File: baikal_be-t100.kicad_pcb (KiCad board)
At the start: 4 copper layers, 95.9 x 90.2 mm, 2 parts, among them J1 2-2013289-1

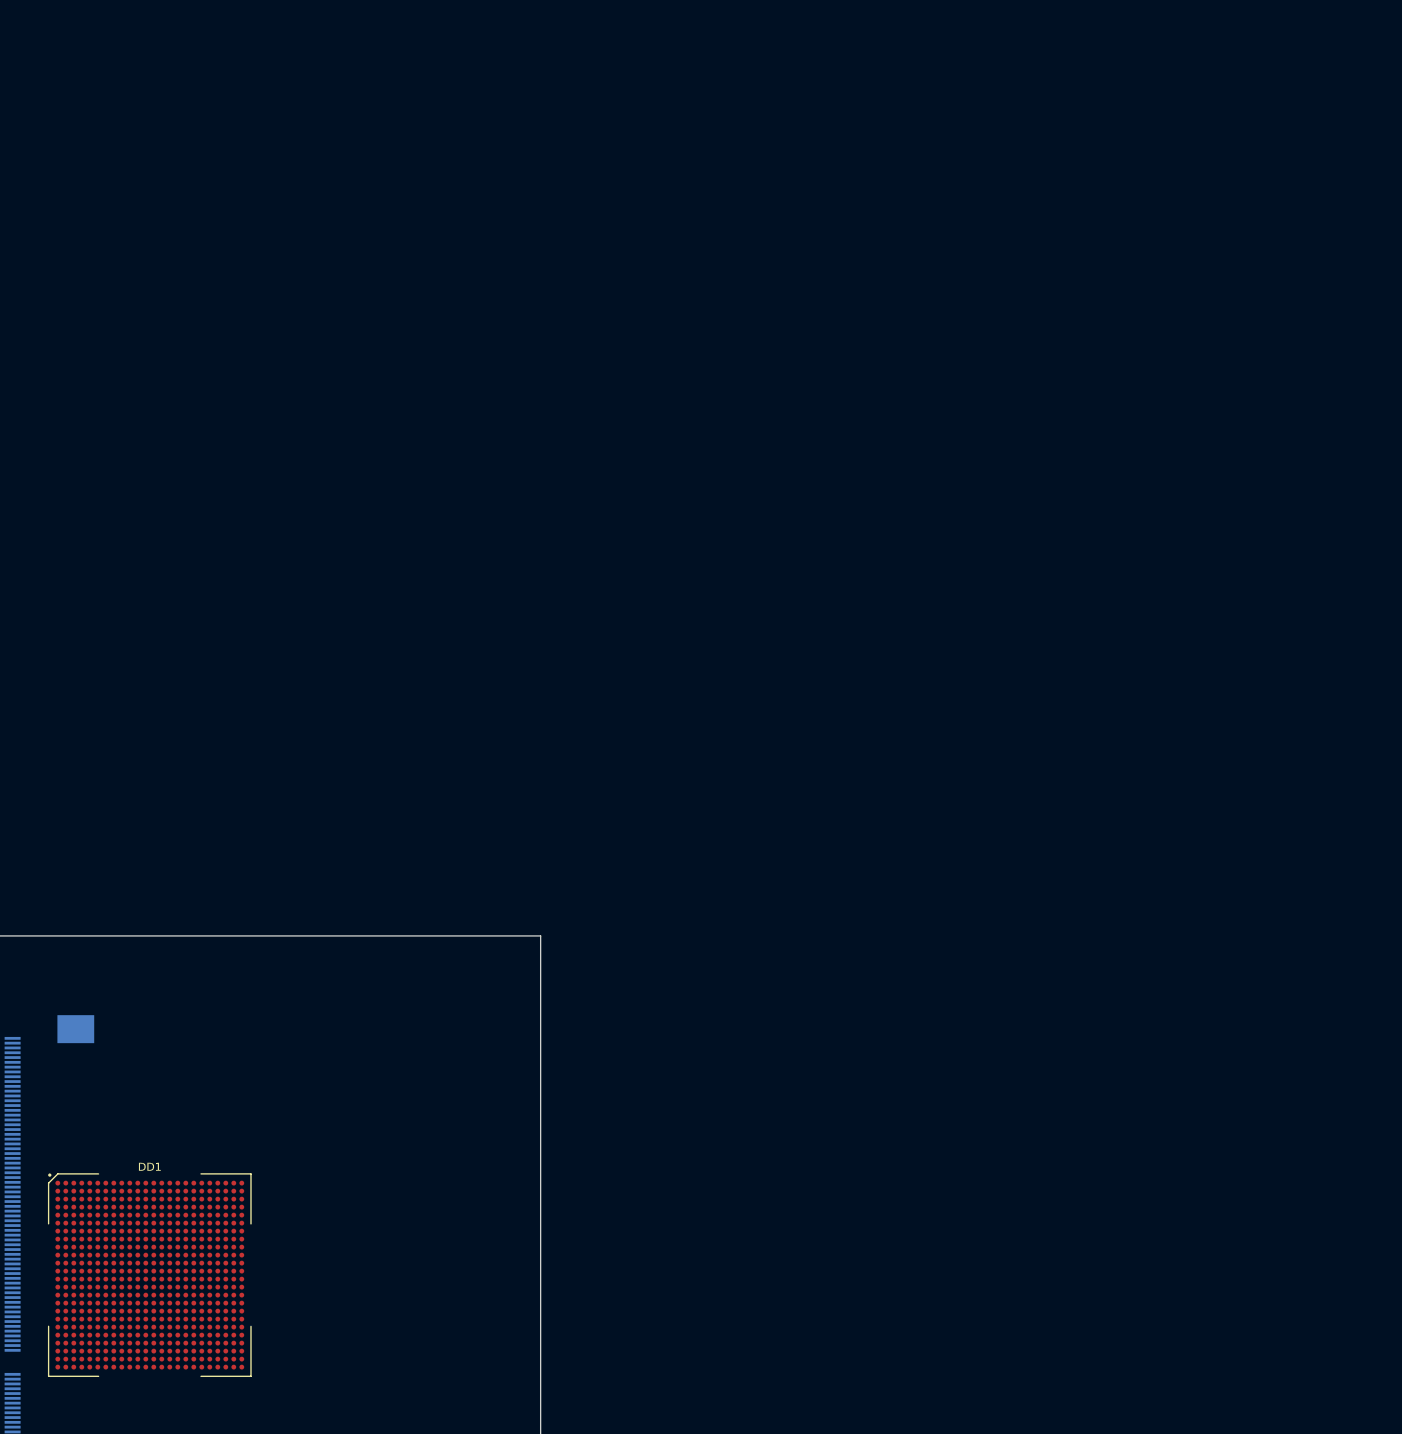
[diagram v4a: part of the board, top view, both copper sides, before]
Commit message: Changes in TRACE, EJTAG, JTAG... Updated CPU symbol.
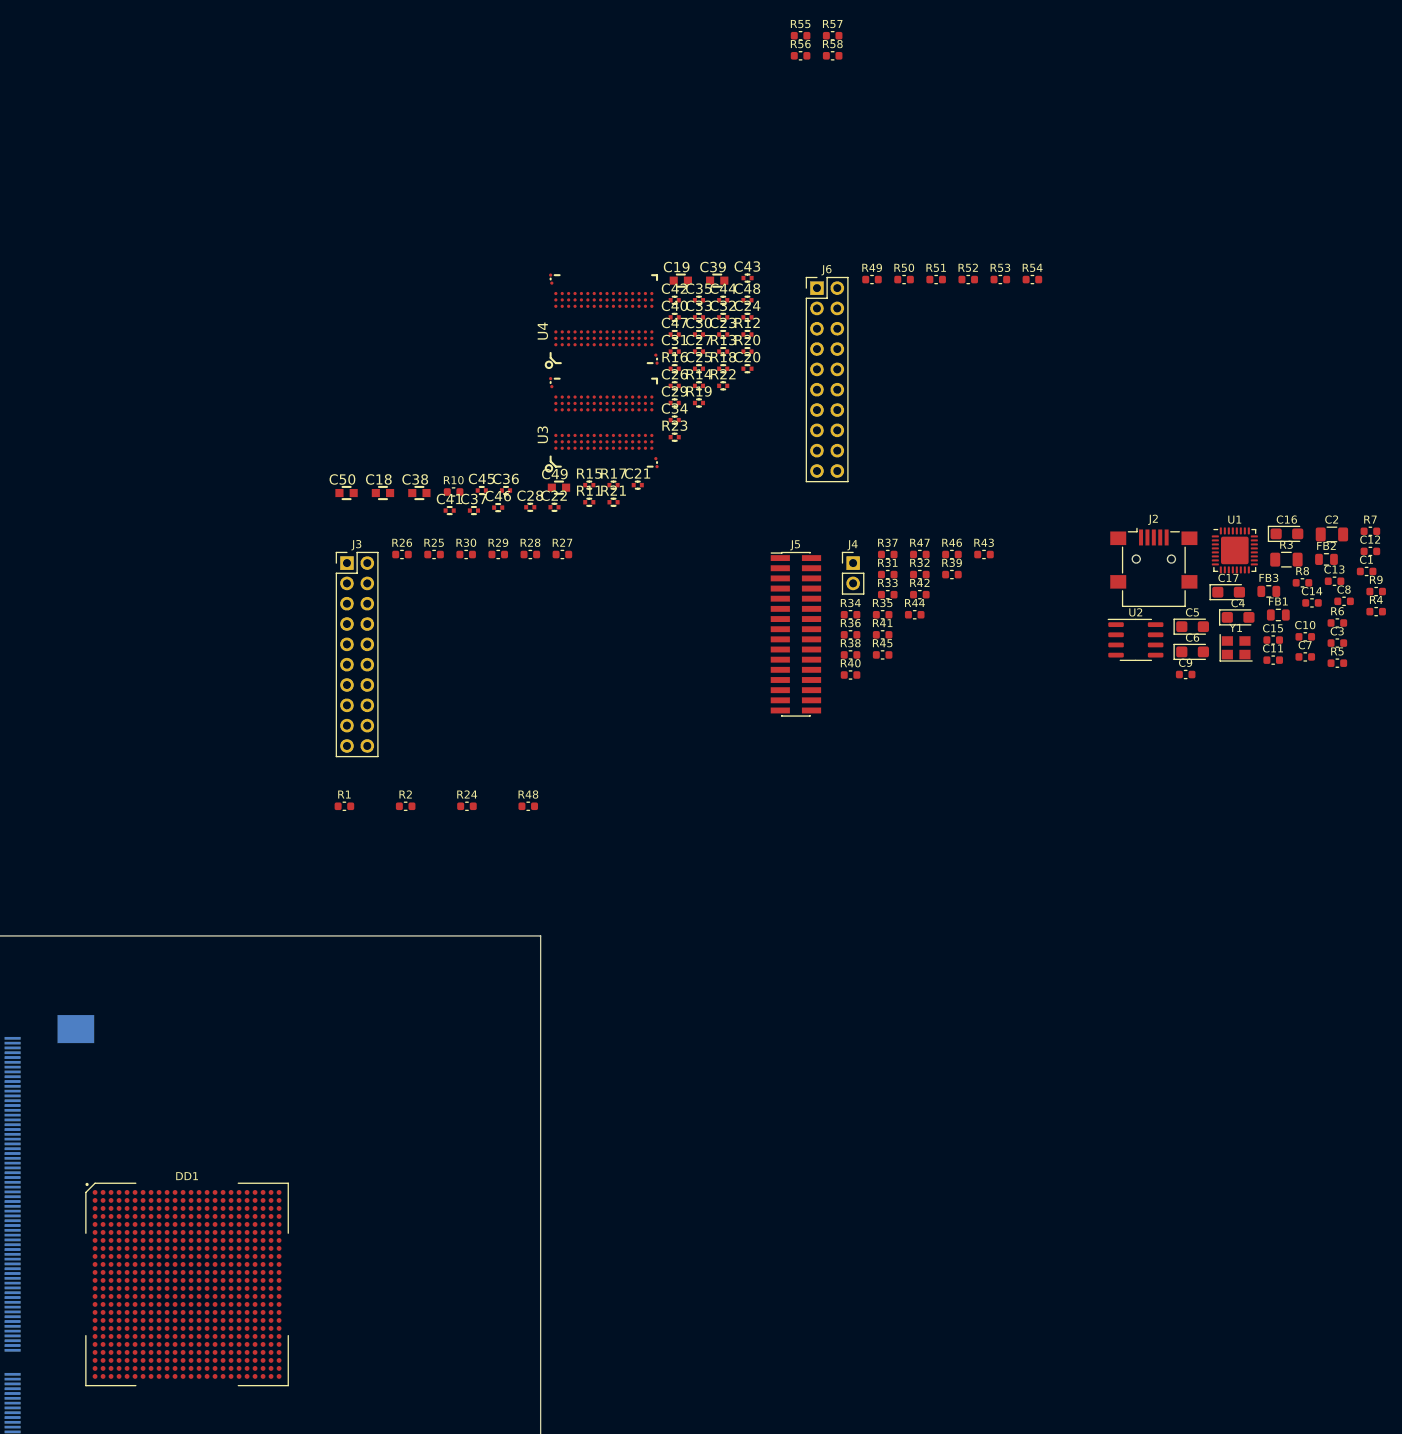
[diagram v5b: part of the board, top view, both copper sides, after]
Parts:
- added C1: 33pF, Capacitor_SMD:C_0603_1608Metric, F.Cu at (103.3, -135.7)
- added C10: 0.01uF, Capacitor_SMD:C_0603_1608Metric, F.Cu at (95.6, -127.6)
- added C11: 0.01uF, Capacitor_SMD:C_0603_1608Metric, F.Cu at (91.6, -124.6)
- added C12: 0.1uF, Capacitor_SMD:C_0603_1608Metric, F.Cu at (103.7, -138.2)
- added C13: 0.1uF, Capacitor_SMD:C_0603_1608Metric, F.Cu at (99.2, -134.5)
- added C14: 0.1uF, Capacitor_SMD:C_0603_1608Metric, F.Cu at (96.4, -131.8)
- added C15: 0.1uF, Capacitor_SMD:C_0603_1608Metric, F.Cu at (91.6, -127.2)
- added C16: 4.7uF/6.3V, Capacitor_Tantalum_SMD:CP_EIA-3216-18_Kemet-A, F.Cu at (93.3, -140.4)
- added C17: 4.7uF/6.3V, Capacitor_Tantalum_SMD:CP_EIA-3216-18_Kemet-A, F.Cu at (86.0, -133.1)
- added C18: 10uF/6.3V/20%, OLIMEX_RLC-FP:C_0603_5MIL_DWS, F.Cu at (-19.7, -145.5)
- added C19: 1uF/10V/10%, OLIMEX_RLC-FP:C_0603_5MIL_DWS, F.Cu at (17.5, -172.1)
- added C2: 0.1uF, Capacitor_SMD:C_1206_3216Metric, F.Cu at (98.9, -140.4)
- added C20: 100nF/10V/10%, OLIMEX_RLC-FP:C_0402_5MIL_DWS, F.Cu at (25.9, -161.1)
- added C21: 100nF/10V/10%, OLIMEX_RLC-FP:C_0402_5MIL_DWS, F.Cu at (12.1, -146.5)
- added C22: 100nF/10V/10%, OLIMEX_RLC-FP:C_0402_5MIL_DWS, F.Cu at (1.73, -143.8)
- added C23: 100nF/10V/10%, OLIMEX_RLC-FP:C_0402_5MIL_DWS, F.Cu at (22.8, -165.4)
- added C24: 100nF/10V/10%, OLIMEX_RLC-FP:C_0402_5MIL_DWS, F.Cu at (25.9, -167.5)
- added C25: 100nF/10V/10%, OLIMEX_RLC-FP:C_0402_5MIL_DWS, F.Cu at (19.8, -161.1)
- added C26: 100nF/10V/10%, OLIMEX_RLC-FP:C_0402_5MIL_DWS, F.Cu at (16.8, -158.9)
- added C27: 100nF/10V/10%, OLIMEX_RLC-FP:C_0402_5MIL_DWS, F.Cu at (19.8, -163.2)
- added C28: 100nF/10V/10%, OLIMEX_RLC-FP:C_0402_5MIL_DWS, F.Cu at (-1.30, -143.8)
- added C29: 100nF/10V/10%, OLIMEX_RLC-FP:C_0402_5MIL_DWS, F.Cu at (16.8, -156.8)
- added C3: 33pF, Capacitor_SMD:C_0603_1608Metric, F.Cu at (99.6, -126.8)
- added C30: 100nF/10V/10%, OLIMEX_RLC-FP:C_0402_5MIL_DWS, F.Cu at (19.8, -165.4)
- added C31: 100nF/10V/10%, OLIMEX_RLC-FP:C_0402_5MIL_DWS, F.Cu at (16.8, -163.2)
- added C32: 100nF/10V/10%, OLIMEX_RLC-FP:C_0402_5MIL_DWS, F.Cu at (22.8, -167.5)
- added C33: 100nF/10V/10%, OLIMEX_RLC-FP:C_0402_5MIL_DWS, F.Cu at (19.8, -167.5)
- added C34: 100nF/10V/10%, OLIMEX_RLC-FP:C_0402_5MIL_DWS, F.Cu at (16.8, -154.7)
- added C35: 100nF/10V/10%, OLIMEX_RLC-FP:C_0402_5MIL_DWS, F.Cu at (19.8, -169.6)
- added C36: 100nF/10V/10%, OLIMEX_RLC-FP:C_0402_5MIL_DWS, F.Cu at (-4.33, -145.9)
- added C37: 100nF/10V/10%, OLIMEX_RLC-FP:C_0402_5MIL_DWS, F.Cu at (-8.34, -143.3)
- added C38: 10uF/6.3V/20%, OLIMEX_RLC-FP:C_0603_5MIL_DWS, F.Cu at (-15.2, -145.5)
- added C39: 10uF/6.3V/20%, OLIMEX_RLC-FP:C_0603_5MIL_DWS, F.Cu at (22.1, -172.1)
- added C4: 10uF/6.3V, Capacitor_Tantalum_SMD:CP_EIA-3216-18_Kemet-A, F.Cu at (87.2, -130.0)
- added C40: 100nF/10V/10%, OLIMEX_RLC-FP:C_0402_5MIL_DWS, F.Cu at (16.8, -167.5)
- added C41: 100nF/10V/10%, OLIMEX_RLC-FP:C_0402_5MIL_DWS, F.Cu at (-11.4, -143.3)
- added C42: 100nF/10V/10%, OLIMEX_RLC-FP:C_0402_5MIL_DWS, F.Cu at (16.8, -169.6)
- added C43: 100nF/10V/10%, OLIMEX_RLC-FP:C_0402_5MIL_DWS, F.Cu at (25.9, -172.4)
- added C44: 100nF/10V/10%, OLIMEX_RLC-FP:C_0402_5MIL_DWS, F.Cu at (22.8, -169.6)
- added C45: 100nF/10V/10%, OLIMEX_RLC-FP:C_0402_5MIL_DWS, F.Cu at (-7.36, -145.9)
- added C46: 100nF/10V/10%, OLIMEX_RLC-FP:C_0402_5MIL_DWS, F.Cu at (-5.31, -143.7)
- added C47: 100nF/10V/10%, OLIMEX_RLC-FP:C_0402_5MIL_DWS, F.Cu at (16.8, -165.4)
- added C48: 100nF/10V/10%, OLIMEX_RLC-FP:C_0402_5MIL_DWS, F.Cu at (25.9, -169.6)
- added C49: 10uF/6.3V/20%, OLIMEX_RLC-FP:C_0603_5MIL_DWS, F.Cu at (2.29, -146.2)
- added C5: 10uF/6.3V, Capacitor_Tantalum_SMD:CP_EIA-3216-18_Kemet-A, F.Cu at (81.5, -128.8)
- added C50: 10uF/6.3V/20%, OLIMEX_RLC-FP:C_0603_5MIL_DWS, F.Cu at (-24.3, -145.5)
- added C6: 10uF/6.3V, Capacitor_Tantalum_SMD:CP_EIA-3216-18_Kemet-A, F.Cu at (81.5, -125.7)
- added C7: 0.1uF, Capacitor_SMD:C_0603_1608Metric, F.Cu at (95.6, -125.0)
- added C8: 0.1uF, Capacitor_SMD:C_0603_1608Metric, F.Cu at (100.4, -132.0)
- added C9: 0.1uF, Capacitor_SMD:C_0603_1608Metric, F.Cu at (80.6, -122.8)
- added FB1: 500mA / 0.1DCR, Inductor_SMD:L_0805_2012Metric, F.Cu at (92.2, -130.3)
- added FB2: 500mA / 0.1DCR, Inductor_SMD:L_0805_2012Metric, F.Cu at (98.2, -137.2)
- added FB3: 500mA / 0.1DCR, Inductor_SMD:L_0805_2012Metric, F.Cu at (91.0, -133.2)
- added J2: USB_OTG, Connector_USB:USB_Mini-B_Lumberg_2486_01_Horizontal, F.Cu at (76.7, -137.3)
- added J3: Conn_02x10_Odd_Even, Connector_PinHeader_2.54mm:PinHeader_2x10_P2.54mm_Vertical, F.Cu at (-24.2, -136.8)
- added J4: Conn_01x02, Connector_PinHeader_2.54mm:PinHeader_1x02_P2.54mm_Vertical, F.Cu at (39.1, -136.8)
- added J5: Conn_02x16_Odd_Even, Connector_PinHeader_1.27mm:PinHeader_2x16_P1.27mm_Vertical_SMD, F.Cu at (31.9, -127.9)
- added J6: Conn_02x10_Odd_Even, Connector_PinHeader_2.54mm:PinHeader_2x10_P2.54mm_Vertical, F.Cu at (34.5, -171.1)
- added R1: 240, Resistor_SMD:R_0603_1608Metric, F.Cu at (-24.5, -106.4)
- added R10: 240, Resistor_SMD:R_0603_1608Metric, F.Cu at (-10.9, -145.7)
- added R11: 22R, OLIMEX_RLC-FP:R_0402_5MIL_DWS, F.Cu at (6.08, -144.4)
- added R12: 22R, OLIMEX_RLC-FP:R_0402_5MIL_DWS, F.Cu at (25.9, -165.4)
- added R13: 2k/1%, OLIMEX_RLC-FP:R_0402_5MIL_DWS, F.Cu at (22.8, -163.2)
- added R14: 2k/1%, OLIMEX_RLC-FP:R_0402_5MIL_DWS, F.Cu at (19.8, -158.9)
- added R15: 2k/1%, OLIMEX_RLC-FP:R_0402_5MIL_DWS, F.Cu at (6.08, -146.5)
- added R16: 2k/1%, OLIMEX_RLC-FP:R_0402_5MIL_DWS, F.Cu at (16.8, -161.1)
- added R17: 243R/1%, OLIMEX_RLC-FP:R_0402_5MIL_DWS, F.Cu at (9.11, -146.5)
- added R18: NA(243R/1%), OLIMEX_RLC-FP:R_0402_5MIL_DWS, F.Cu at (22.8, -161.1)
- added R19: 2k/1%, OLIMEX_RLC-FP:R_0402_5MIL_DWS, F.Cu at (19.8, -156.8)
- added R2: 200, Resistor_SMD:R_0603_1608Metric, F.Cu at (-16.9, -106.4)
- added R20: 100R/1%, OLIMEX_RLC-FP:R_0402_5MIL_DWS, F.Cu at (25.9, -163.2)
- added R21: NA, OLIMEX_RLC-FP:R_0402_5MIL_DWS, F.Cu at (9.11, -144.4)
- added R22: 243R/1%, OLIMEX_RLC-FP:R_0402_5MIL_DWS, F.Cu at (22.8, -158.9)
- added R23: NA(243R/1%), OLIMEX_RLC-FP:R_0402_5MIL_DWS, F.Cu at (16.8, -152.5)
- added R24: 33, Resistor_SMD:R_0603_1608Metric, F.Cu at (-9.21, -106.4)
- added R25: 47K, Resistor_SMD:R_0603_1608Metric, F.Cu at (-13.3, -137.8)
- added R26: 47K, Resistor_SMD:R_0603_1608Metric, F.Cu at (-17.3, -137.8)
- added R27: 47K, Resistor_SMD:R_0603_1608Metric, F.Cu at (2.72, -137.8)
- added R28: 47K, Resistor_SMD:R_0603_1608Metric, F.Cu at (-1.29, -137.8)
- added R29: 47K, Resistor_SMD:R_0603_1608Metric, F.Cu at (-5.30, -137.8)
- added R3: 1M, Resistor_SMD:R_1206_3216Metric, F.Cu at (93.2, -137.2)
- added R30: 47K, Resistor_SMD:R_0603_1608Metric, F.Cu at (-9.31, -137.8)
- added R31: 33, Resistor_SMD:R_0603_1608Metric, F.Cu at (43.4, -135.3)
- added R32: 33, Resistor_SMD:R_0603_1608Metric, F.Cu at (47.4, -135.3)
- added R33: 33, Resistor_SMD:R_0603_1608Metric, F.Cu at (43.4, -132.8)
- added R34: 33, Resistor_SMD:R_0603_1608Metric, F.Cu at (38.7, -130.3)
- added R35: 33, Resistor_SMD:R_0603_1608Metric, F.Cu at (42.8, -130.3)
- added R36: 33, Resistor_SMD:R_0603_1608Metric, F.Cu at (38.7, -127.8)
- added R37: 33, Resistor_SMD:R_0603_1608Metric, F.Cu at (43.4, -137.8)
- added R38: 33, Resistor_SMD:R_0603_1608Metric, F.Cu at (38.7, -125.3)
- added R39: 33, Resistor_SMD:R_0603_1608Metric, F.Cu at (51.4, -135.3)
- added R4: 1M, Resistor_SMD:R_0603_1608Metric, F.Cu at (104.4, -130.7)
- added R40: 33, Resistor_SMD:R_0603_1608Metric, F.Cu at (38.7, -122.8)
- added R41: 33, Resistor_SMD:R_0603_1608Metric, F.Cu at (42.8, -127.8)
- added R42: 33, Resistor_SMD:R_0603_1608Metric, F.Cu at (47.4, -132.8)
- added R43: 33, Resistor_SMD:R_0603_1608Metric, F.Cu at (55.4, -137.8)
- added R44: 33, Resistor_SMD:R_0603_1608Metric, F.Cu at (46.8, -130.3)
- added R45: 33, Resistor_SMD:R_0603_1608Metric, F.Cu at (42.8, -125.3)
- added R46: 33, Resistor_SMD:R_0603_1608Metric, F.Cu at (51.4, -137.8)
- added R47: 4K7, Resistor_SMD:R_0603_1608Metric, F.Cu at (47.4, -137.8)
- added R48: 33, Resistor_SMD:R_0603_1608Metric, F.Cu at (-1.55, -106.4)
- added R49: 47K, Resistor_SMD:R_0603_1608Metric, F.Cu at (41.4, -172.2)
- added R5: 12K, Resistor_SMD:R_0603_1608Metric, F.Cu at (99.6, -124.3)
- added R50: 47K, Resistor_SMD:R_0603_1608Metric, F.Cu at (45.4, -172.2)
- added R51: 47K, Resistor_SMD:R_0603_1608Metric, F.Cu at (49.4, -172.2)
- added R52: 47K, Resistor_SMD:R_0603_1608Metric, F.Cu at (53.5, -172.2)
- added R53: 47K, Resistor_SMD:R_0603_1608Metric, F.Cu at (57.5, -172.2)
- added R54: 47K, Resistor_SMD:R_0603_1608Metric, F.Cu at (61.5, -172.2)
- added R55: 33, Resistor_SMD:R_0603_1608Metric, F.Cu at (32.5, -202.7)
- added R56: 33, Resistor_SMD:R_0603_1608Metric, F.Cu at (32.5, -200.2)
- added R57: 33, Resistor_SMD:R_0603_1608Metric, F.Cu at (36.5, -202.7)
- added R58: 4K7, Resistor_SMD:R_0603_1608Metric, F.Cu at (36.5, -200.2)
- added R6: 0, Resistor_SMD:R_0603_1608Metric, F.Cu at (99.6, -129.3)
- added R7: 0, Resistor_SMD:R_0603_1608Metric, F.Cu at (103.7, -140.7)
- added R8: 4K7, Resistor_SMD:R_0603_1608Metric, F.Cu at (95.2, -134.3)
- added R9: 4K7, Resistor_SMD:R_0603_1608Metric, F.Cu at (104.4, -133.2)
- added U1: USB3300-EZK, Package_DFN_QFN:QFN-32-1EP_5x5mm_P0.5mm_EP3.45x3.45mm, F.Cu at (86.8, -138.4)
- added U2: MIC2025-1YM, Package_SO:SOIC-8_3.9x4.9mm_P1.27mm, F.Cu at (74.4, -127.2)
- added U3: K4B4G1646Q-HYK0(FBGA-96_256Mx16_DDR3-1600_11-11-11), OLIMEX_IC-FP:FBGA96(HYNIX_SAMSUNG_512MX16_DDR3), F.Cu at (7.90, -154.3)
- added U4: K4B4G1646Q-HYK0(FBGA-96_256Mx16_DDR3-1600_11-11-11), OLIMEX_IC-FP:FBGA96(HYNIX_SAMSUNG_512MX16_DDR3), F.Cu at (7.90, -167.3)
- added Y1: 24MHz, Crystal:Crystal_SMD_3225-4Pin_3.2x2.5mm, F.Cu at (86.9, -126.2)
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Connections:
- DD1 pad A10: (no net) -> Net-(DD1-PadA10)
- DD1 pad A11: (no net) -> Net-(DD1-PadA11)
- DD1 pad A12: (no net) -> Net-(DD1-PadA12)
- DD1 pad A13: (no net) -> /CPU/DEBUG/CPU_EJTAG/EJTAG20_Conn/TCK
- DD1 pad A14: (no net) -> /CPU/DEBUG/CPU_EJTAG/EJTAG20_Conn/DBGRQ
- DD1 pad A24: +1V5 -> +1V8
- DD1 pad A9: (no net) -> Net-(DD1-PadA9)
- DD1 pad AA1: (no net) -> /CPU/DEBUG/CPU_JTAG/JTAG20_Conn/TCK
- DD1 pad AA19: /CPU/DDR3/DQ0 -> /CPU/DDR3_chip/S0SDQ0
- DD1 pad AA2: (no net) -> /CPU/DEBUG/CPU_JTAG/JTAG20_Conn/TMS
- DD1 pad AA20: (no net) -> /CPU/DDR3_chip/S0SDQ5
- DD1 pad AA21: (no net) -> /CPU/DDR3_chip/S0SDQ7
- DD1 pad AA22: /CPU/DDR3/DQ1 -> /CPU/DDR3_chip/S0SDQ1
- DD1 pad AA23: (no net) -> /CPU/DDR3_chip/S0SDQ14
- DD1 pad AA24: (no net) -> /CPU/DDR3_chip/S0SDQ13
- DD1 pad AA5: (no net) -> Net-(DD1-PadAA5)
- DD1 pad AB1: (no net) -> /CPU/DEBUG/CPU_JTAG/JTAG20_Conn/TDO
- DD1 pad AB2: (no net) -> /CPU/DEBUG/CPU_JTAG/JTAG20_Conn/TDI
- DD1 pad AB23: /CPU/DDR3/DQ2 -> /CPU/DDR3_chip/S0SDQ2
- DD1 pad AB24: /CPU/DDR3/DQ3 -> /CPU/DDR3_chip/S0SDQ3
- DD1 pad AB3: Net-(DD1-PadAB3) -> +1V8
- DD1 pad AC22: /CPU/DDR3/DM0 -> /CPU/DDR3_chip/S0SDQM0
- DD1 pad AC23: (no net) -> /CPU/DDR3_chip/S0SDQS0_P
- DD1 pad AC24: (no net) -> /CPU/DDR3_chip/S0SDQS0_N
- DD1 pad AD21: (no net) -> /CPU/DDR3_chip/S0SDQ6
- DD1 pad AD22: (no net) -> /CPU/DDR3_chip/S0SDQ4
- DD1 pad AD24: +1V5 -> +1V8
- DD1 pad B10: (no net) -> Net-(DD1-PadB10)
- DD1 pad B11: (no net) -> Net-(DD1-PadB11)
- DD1 pad B12: (no net) -> Net-(DD1-PadB12)
- DD1 pad B13: (no net) -> /CPU/DEBUG/CPU_EJTAG/EJTAG20_Conn/nTRST
- DD1 pad B14: (no net) -> /CPU/DEBUG/CPU_EJTAG/EJTAG20_Conn/TMS
- DD1 pad B9: (no net) -> Net-(DD1-PadB9)
- DD1 pad C10: Net-(DD1-PadAB3) -> +1V8
- DD1 pad C11: (no net) -> Net-(DD1-PadC11)
- DD1 pad C12: Net-(DD1-PadAB3) -> +1V8
- DD1 pad C13: (no net) -> Net-(DD1-PadC13)
- DD1 pad C14: (no net) -> /CPU/DEBUG/CPU_EJTAG/EJTAG20_Conn/TDI
- DD1 pad C19: (no net) -> Net-(DD1-PadC19)
- DD1 pad C4: Net-(DD1-PadAB3) -> +1V8
- DD1 pad C6: Net-(DD1-PadAB3) -> +1V8
- DD1 pad C7: Net-(DD1-PadAB3) -> +1V8
- DD1 pad C8: (no net) -> Net-(DD1-PadC8)
- DD1 pad C9: (no net) -> Net-(DD1-PadC9)
- DD1 pad D11: (no net) -> Net-(DD1-PadD11)
- DD1 pad D13: (no net) -> /CPU/DEBUG/CPU_TRACE/TR_TRIGIN
- DD1 pad D9: (no net) -> Net-(DD1-PadD9)
- DD1 pad E10: (no net) -> Net-(DD1-PadE10)
- DD1 pad E11: (no net) -> Net-(DD1-PadE11)
- DD1 pad E12: (no net) -> Net-(DD1-PadE12)
- DD1 pad E13: (no net) -> /CPU/DEBUG/CPU_TRACE/TR_PROBE_N
- DD1 pad E18: (no net) -> /CPU/DDR3_chip/S0SVREF
- DD1 pad E20: (no net) -> /CPU/DDR3_chip/S0SDQ27
- DD1 pad E21: (no net) -> /CPU/DDR3_chip/S0SDQ25
- DD1 pad E22: (no net) -> /CPU/DDR3_chip/S0SDQ26
- DD1 pad E23: (no net) -> /CPU/DDR3_chip/S0SDQ30
- DD1 pad E24: (no net) -> /CPU/DDR3_chip/S0SDQ29
- DD1 pad F11: (no net) -> Net-(DD1-PadF11)
- DD1 pad F12: (no net) -> Net-(DD1-PadF12)
- DD1 pad F13: (no net) -> Net-(DD1-PadF13)
- DD1 pad F14: (no net) -> /CPU/DEBUG/CPU_TRACE/TR_TEST
- DD1 pad F20: (no net) -> /CPU/DDR3_chip/S0SDQ31
- DD1 pad F21: (no net) -> /CPU/DDR3_chip/S0SDQ28
- DD1 pad F22: (no net) -> /CPU/DDR3_chip/S0SDQM3
- DD1 pad F23: (no net) -> /CPU/DDR3_chip/S0SDQS3_P
- DD1 pad F24: (no net) -> /CPU/DDR3_chip/S0SDQS3_N
- DD1 pad F3: Net-(DD1-PadAB3) -> +1V8
- DD1 pad G19: (no net) -> /CPU/DDR3_chip/S0SWE
- DD1 pad G20: (no net) -> /CPU/DDR3_chip/S0SBA2
- DD1 pad G21: (no net) -> /CPU/DDR3_chip/S0SDQ24
- DD1 pad G24: +1V5 -> +1V8
- DD1 pad H17: (no net) -> /CPU/DDR3_chip/S0SVREF
- DD1 pad H20: (no net) -> /CPU/DDR3_chip/S0SCKE1
- DD1 pad H21: (no net) -> /CPU/DDR3_chip/S0SRAS
- DD1 pad H22: (no net) -> /CPU/DDR3_chip/S0SA10
- DD1 pad H23: (no net) -> /CPU/DDR3_chip/S0SCS0
- DD1 pad H24: (no net) -> /CPU/DDR3_chip/S0SODT0
- DD1 pad H3: Net-(DD1-PadAB3) -> +1V8
- DD1 pad J17: (no net) -> Net-(DD1-PadJ17)
- DD1 pad J18: (no net) -> /CPU/DDR3_chip/S0SVREF
- DD1 pad J19: (no net) -> /CPU/DDR3_chip/S0SBA1
- DD1 pad J20: (no net) -> /CPU/DDR3_chip/S0SCS1
- DD1 pad J21: (no net) -> /CPU/DDR3_chip/S0SA15
- DD1 pad J22: (no net) -> /CPU/DDR3_chip/S0SCAS
- DD1 pad K18: (no net) -> /CPU/DDR3_chip/S0SA12
- DD1 pad K19: (no net) -> /CPU/DDR3_chip/S0SA0
- DD1 pad K2: (no net) -> /CPU/ULPI/ULPI_CLK
- DD1 pad K22: (no net) -> /CPU/DDR3_chip/S0SA2
- DD1 pad K23: (no net) -> /CPU/DDR3_chip/S0SCKE0
- DD1 pad K24: (no net) -> /CPU/DDR3_chip/S0SA1
- DD1 pad K3: (no net) -> /CPU/ULPI/ULPI_DIR
- DD1 pad K4: (no net) -> /CPU/ULPI/ULPI_NXT
- DD1 pad K5: (no net) -> /CPU/ULPI/EXTBUS_FLG
- DD1 pad L1: (no net) -> /CPU/ULPI/ULPI_DATA0
- DD1 pad L2: (no net) -> /CPU/ULPI/ULPI_DATA1
- DD1 pad L20: (no net) -> /CPU/DDR3_chip/S0SA14
- DD1 pad L3: Net-(DD1-PadAB3) -> +1V8
- DD1 pad L5: (no net) -> /CPU/ULPI/ULPI_DATA2
- DD1 pad L6: (no net) -> /CPU/ULPI/ULPI_STP
- DD1 pad L7: (no net) -> /CPU/ULPI/USB_VBUS
- DD1 pad M17: (no net) -> /CPU/DDR3_chip/S0SVREF
- DD1 pad M18: (no net) -> /CPU/DDR3_chip/S0SA4
- DD1 pad M19: (no net) -> /CPU/DDR3_chip/S0SA13
- DD1 pad M20: (no net) -> /CPU/DDR3_chip/S0SA11
- DD1 pad M21: (no net) -> /CPU/DDR3_chip/S0SA9
- DD1 pad M22: (no net) -> /CPU/DDR3_chip/S0SA3
- DD1 pad M23: (no net) -> Net-(DD1-PadM23)
- DD1 pad M24: (no net) -> Net-(DD1-PadM24)
- DD1 pad M3: (no net) -> /CPU/ULPI/ULPI_DATA6
- DD1 pad M4: (no net) -> /CPU/ULPI/ULPI_DATA7
- DD1 pad M5: (no net) -> /CPU/ULPI/ULPI_DATA3
- DD1 pad M6: (no net) -> /CPU/ULPI/ULPI_DATA4
- DD1 pad M7: (no net) -> /CPU/ULPI/ULPI_DATA5
- DD1 pad N19: (no net) -> /CPU/DDR3_chip/S0SA6
- DD1 pad N22: (no net) -> /CPU/DDR3_chip/S0SBA0
- DD1 pad P19: (no net) -> /CPU/DDR3_chip/S0SA7
- DD1 pad P20: (no net) -> /CPU/DDR3_chip/S0SA8
- DD1 pad P21: (no net) -> /CPU/DDR3_chip/S0SA5
- DD1 pad P22: (no net) -> /CPU/DDR3_chip/S0SODT1
- DD1 pad P23: /CPU/DDR3/DQ17 -> /CPU/DDR3_chip/S0SDQ17
- DD1 pad P24: /CPU/DDR3/DQ18 -> /CPU/DDR3_chip/S0SDQ18
- DD1 pad P3: Net-(DD1-PadAB3) -> +1V8
- DD1 pad R18: (no net) -> /CPU/DDR3_chip/S0SVREF
- DD1 pad R21: /CPU/DDR3/DQ19 -> /CPU/DDR3_chip/S0SDQ19
- DD1 pad R24: +1V5 -> +1V8
- DD1 pad T19: (no net) -> /CPU/DDR3_chip/S0SRST
- DD1 pad T20: (no net) -> /CPU/DDR3_chip/S0SDQ23
- DD1 pad T21: (no net) -> /CPU/DDR3_chip/S0SDQ20
- DD1 pad T22: (no net) -> /CPU/DDR3_chip/S0SDQM2
- DD1 pad T23: /CPU/DDR3/DQS2 -> /CPU/DDR3_chip/S0SDQS2_P
- DD1 pad T24: /CPU/DDR3/DQS_N2 -> /CPU/DDR3_chip/S0SDQS2_N
- DD1 pad T3: Net-(DD1-PadAB3) -> +1V8
- DD1 pad U18: (no net) -> /CPU/DDR3_chip/S0SVREF
- DD1 pad U21: (no net) -> /CPU/DDR3_chip/S0SDQ22
- DD1 pad U24: (no net) -> /CPU/DDR3_chip/S0SDQ21
- DD1 pad U3: (no net) -> /CPU/DEBUG/CPU_TRACE/TSTSEL_3
- DD1 pad V20: /CPU/DDR3/DQ16 -> /CPU/DDR3_chip/S0SDQ16
- DD1 pad V21: (no net) -> /CPU/DDR3_chip/S0SDQ15
- DD1 pad V22: /CPU/DDR3/DQ8 -> /CPU/DDR3_chip/S0SDQ8
- DD1 pad V23: /CPU/DDR3/DQ9 -> /CPU/DDR3_chip/S0SDQ9
- DD1 pad V24: /CPU/DDR3/DQ10 -> /CPU/DDR3_chip/S0SDQ10
- DD1 pad W19: (no net) -> /CPU/DDR3_chip/S0SVREF
- DD1 pad W21: (no net) -> /CPU/DDR3_chip/S0SDQM1
- DD1 pad W24: +1V5 -> +1V8
- DD1 pad W3: Net-(DD1-PadAB3) -> +1V8
- DD1 pad Y17: Net-(DD1-PadAB3) -> +1V8
- DD1 pad Y21: (no net) -> /CPU/DDR3_chip/S0SDQ12
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
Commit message: Added some footprints
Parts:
- added C1: 0.1uF, Capacitor_SMD:C_0603_1608Metric, F.Cu at (148.5, -46.2)
- added C10: 0.1uF, Capacitor_SMD:C_0603_1608Metric, F.Cu at (130.3, -35.2)
- added C100: 0.01uF, Capacitor_SMD:C_0402_1005Metric, F.Cu at (160.8, -89.5)
- added C101: 0.01uF, Capacitor_SMD:C_0402_1005Metric, F.Cu at (163.7, -90.5)
- added C102: 0.01uF, Capacitor_SMD:C_0402_1005Metric, F.Cu at (168.1, -93.0)
- added C103: 0.01uF, Capacitor_SMD:C_0402_1005Metric, F.Cu at (163.7, -88.5)
- added C104: 0.01uF, Capacitor_SMD:C_0402_1005Metric, F.Cu at (166.6, -90.5)
- added C105: 0.01uF, Capacitor_SMD:C_0402_1005Metric, F.Cu at (166.7, -95.0)
- added C106: 0.01uF, Capacitor_SMD:C_0402_1005Metric, F.Cu at (153.9, -86.6)
- added C107: 0.01uF, Capacitor_SMD:C_0402_1005Metric, F.Cu at (157.9, -89.5)
- added C108: 10uF/6.3V/0603, Capacitor_SMD:C_0603_1608Metric, F.Cu at (154.4, -88.8)
- added C109: 4.7uF/10V/0402, Capacitor_SMD:C_0402_1005Metric, F.Cu at (152.8, -84.1)
- added C11: 0.1uF, Capacitor_SMD:C_0603_1608Metric, F.Cu at (148.3, -26.0)
- added C110: 0.1uF/10V/0402, Capacitor_SMD:C_0402_1005Metric, F.Cu at (162.3, -92.5)
- added C111: 0.01uF/10V/0402, Capacitor_SMD:C_0402_1005Metric, F.Cu at (156.8, -86.6)
- added C112: 10uF/6.3V/0603, Capacitor_SMD:C_0603_1608Metric, F.Cu at (163.3, -94.7)
- added C113: 4.7uF/10V/0402, Capacitor_SMD:C_0402_1005Metric, F.Cu at (159.7, -85.6)
- added C114: 0.1uF/10V/0402, Capacitor_SMD:C_0402_1005Metric, F.Cu at (155.7, -84.6)
- added C115: 0.01uF/10V/0402, Capacitor_SMD:C_0402_1005Metric, F.Cu at (149.9, -84.1)
- added C116: 10uF/6.3V/0603, Capacitor_SMD:C_0603_1608Metric, F.Cu at (158.9, -91.8)
- added C117: 4.7uF/10V/0402, Capacitor_SMD:C_0402_1005Metric, F.Cu at (165.2, -92.5)
- added C118: 0.1uF/10V/0402, Capacitor_SMD:C_0402_1005Metric, F.Cu at (159.7, -87.6)
- added C119: 0.01uF/10V/0402, Capacitor_SMD:C_0402_1005Metric, F.Cu at (169.6, -95.0)
- added C12: 0.1uF, Capacitor_SMD:C_0603_1608Metric, F.Cu at (140.3, -26.0)
- added C120: 0.1uF/16V/X7R, Capacitor_SMD:C_0603_1608Metric, F.Cu at (195.2, -57.4)
- added C121: 0.1uF/16V/X7R, Capacitor_SMD:C_0603_1608Metric, F.Cu at (195.2, -59.9)
- added C122: 0.1uF/16V/X7R, Capacitor_SMD:C_0603_1608Metric, F.Cu at (195.5, -67.7)
- added C123: 0.1uF/16V/X7R, Capacitor_SMD:C_0603_1608Metric, F.Cu at (195.5, -70.2)
- added C124: 1uF, Capacitor_SMD:C_0805_2012Metric, F.Cu at (122.7, -42.1)
- added C125: 0.01uF, Capacitor_SMD:C_0603_1608Metric, F.Cu at (131.8, -46.8)
- added C126: 12pF, Capacitor_SMD:C_0603_1608Metric, F.Cu at (126.9, -42.3)
- added C127: 12pF, Capacitor_SMD:C_0603_1608Metric, F.Cu at (130.9, -42.8)
- added C13: 0.1uF, Capacitor_SMD:C_0603_1608Metric, F.Cu at (179.6, -59.9)
- added C14: 0.1uF, Capacitor_SMD:C_0603_1608Metric, F.Cu at (187.6, -59.9)
- added C145: 10uF/6.3V/0603, Capacitor_SMD:C_0603_1608Metric, F.Cu at (163.0, -56.0)
- added C146: 4.7uF/10V/0402, Capacitor_SMD:C_0402_1005Metric, F.Cu at (166.5, -54.2)
- added C147: 0.1uF/10V/0402, Capacitor_SMD:C_0402_1005Metric, F.Cu at (169.4, -56.2)
- added C148: 0.01uF/10V/0402, Capacitor_SMD:C_0402_1005Metric, F.Cu at (165.4, -51.2)
- added C149: 10uF/6.3V/0603, Capacitor_SMD:C_0603_1608Metric, F.Cu at (163.0, -53.5)
- added C15: 0.1uF, Capacitor_SMD:C_0603_1608Metric, F.Cu at (158.5, -32.0)
- added C150: 4.7uF/10V/0402, Capacitor_SMD:C_0402_1005Metric, F.Cu at (162.5, -51.2)
- added C151: 0.1uF/10V/0402, Capacitor_SMD:C_0402_1005Metric, F.Cu at (166.5, -56.2)
- added C152: 0.01uF/10V/0402, Capacitor_SMD:C_0402_1005Metric, F.Cu at (158.0, -50.3)
- added C153: 10uF/6.3V/0603, Capacitor_SMD:C_0603_1608Metric, F.Cu at (126.0, -77.2)
- added C154: 1uF/10V/0402, Capacitor_SMD:C_0603_1608Metric, F.Cu at (121.6, -74.3)
- added C155: 0.1uF/10V/0402, Capacitor_SMD:C_0402_1005Metric, F.Cu at (125.1, -74.5)
- added C156: 0.01uF/10V/0402, Capacitor_SMD:C_0402_1005Metric, F.Cu at (129.5, -77.5)
- added C157: 0.01uF/10V/0402, Capacitor_SMD:C_0402_1005Metric, F.Cu at (128.0, -75.0)
- added C158: 10nF, chip_rlc:c_0201, F.Cu at (58.5, -17.2)
- added C159: 10nF, chip_rlc:c_0201, F.Cu at (60.3, -17.2)
- added C16: 0.1uF, Capacitor_SMD:C_0603_1608Metric, F.Cu at (162.5, -34.6)
- added C160: 100nF, chip_rlc:c_0201, F.Cu at (62.1, -17.2)
- added C161: 100nF, chip_rlc:c_0201, F.Cu at (63.9, -17.2)
- added C162: 100nF, chip_rlc:c_0201, F.Cu at (58.5, -15.7)
- added C163: 10nF, chip_rlc:c_0201, F.Cu at (60.3, -15.7)
- added C164: 10nF, chip_rlc:c_0201, F.Cu at (62.1, -15.7)
- added C165: 10nF, chip_rlc:c_0201, F.Cu at (58.5, -14.2)
- added C166: 100nF, chip_rlc:c_0201, F.Cu at (60.3, -14.2)
- added C167: 100nF, chip_rlc:c_0201, F.Cu at (58.5, -12.7)
- added C17: 0.1uF, Capacitor_SMD:C_0603_1608Metric, F.Cu at (154.7, -77.2)
- added C2: 0.1uF, Capacitor_SMD:C_0603_1608Metric, F.Cu at (148.5, -48.7)
- added C3: 0.1uF, Capacitor_SMD:C_0603_1608Metric, F.Cu at (169.6, -64.8)
- added C4: 0.1uF, Capacitor_SMD:C_0603_1608Metric, F.Cu at (169.6, -67.3)
- added C5: 0.1uF, Capacitor_SMD:C_0603_1608Metric, F.Cu at (169.6, -78.7)
- added C51: 0.1uF, Capacitor_SMD:C_0603_1608Metric, F.Cu at (179.3, -34.6)
- added C52: 0.1uF, Capacitor_SMD:C_0603_1608Metric, F.Cu at (146.0, -54.9)
- added C53: 22uF, Capacitor_SMD:C_0805_2012Metric, F.Cu at (137.4, -54.7)
- added C54: 0.1uF, Capacitor_SMD:C_0603_1608Metric, F.Cu at (151.1, -62.1)
- added C55: 1uF, Capacitor_SMD:C_0805_2012Metric, F.Cu at (141.8, -54.7)
- added C56: 100uF, Capacitor_SMD:C_1206_3216Metric, F.Cu at (128.0, -87.8)
- added C57: 100uF, Capacitor_SMD:C_1206_3216Metric, F.Cu at (122.4, -84.5)
- added C58: 100uF, Capacitor_SMD:C_1206_3216Metric, F.Cu at (133.6, -94.4)
- added C59: 100uF, Capacitor_SMD:C_1206_3216Metric, F.Cu at (128.0, -91.1)
- added C6: 0.1uF, Capacitor_SMD:C_0603_1608Metric, F.Cu at (169.6, -76.1)
- added C60: 100uF, Capacitor_SMD:C_1206_3216Metric, F.Cu at (122.4, -87.8)
- added C61: 100uF, Capacitor_SMD:C_1206_3216Metric, F.Cu at (128.0, -94.4)
- added C62: 100uF, Capacitor_SMD:C_1206_3216Metric, F.Cu at (122.4, -91.1)
- added C63: 100uF, Capacitor_SMD:C_1206_3216Metric, F.Cu at (122.4, -94.4)
- added C64: 4.7uF, Capacitor_SMD:C_0402_1005Metric, F.Cu at (143.7, -95.0)
- added C65: 4.7uF, Capacitor_SMD:C_0402_1005Metric, F.Cu at (137.9, -95.0)
- added C66: 4.7uF, Capacitor_SMD:C_0402_1005Metric, F.Cu at (132.3, -89.7)
- added C67: 4.7uF, Capacitor_SMD:C_0402_1005Metric, F.Cu at (132.3, -91.7)
- added C68: 1uF, Capacitor_SMD:C_0402_1005Metric, F.Cu at (126.7, -83.1)
- added C69: 1uF, Capacitor_SMD:C_0402_1005Metric, F.Cu at (135.2, -91.7)
- added C7: 0.1uF, Capacitor_SMD:C_0603_1608Metric, F.Cu at (148.5, -34.8)
- added C70: 1uF, Capacitor_SMD:C_0402_1005Metric, F.Cu at (129.6, -85.1)
- added C71: 1uF, Capacitor_SMD:C_0402_1005Metric, F.Cu at (132.3, -87.7)
- added C72: 0.22uF, Capacitor_SMD:C_0402_1005Metric, F.Cu at (135.2, -87.7)
- added C73: 0.22uF, Capacitor_SMD:C_0402_1005Metric, F.Cu at (138.1, -91.0)
- added C74: 0.22uF, Capacitor_SMD:C_0402_1005Metric, F.Cu at (141.0, -89.0)
- added C75: 0.22uF, Capacitor_SMD:C_0402_1005Metric, F.Cu at (135.4, -83.8)
- added C76: 0.1uF, Capacitor_SMD:C_0402_1005Metric, F.Cu at (143.9, -93.0)
- added C77: 0.1uF, Capacitor_SMD:C_0402_1005Metric, F.Cu at (141.0, -91.0)
- added C78: 0.1uF, Capacitor_SMD:C_0402_1005Metric, F.Cu at (132.5, -83.8)
- added C79: 0.1uF, Capacitor_SMD:C_0402_1005Metric, F.Cu at (141.0, -93.0)
- added C8: 0.1uF, Capacitor_SMD:C_0603_1608Metric, F.Cu at (148.5, -37.4)
- added C80: 0.1uF, Capacitor_SMD:C_0402_1005Metric, F.Cu at (138.1, -89.0)
- added C81: 0.1uF, Capacitor_SMD:C_0402_1005Metric, F.Cu at (135.4, -85.7)
- added C82: 0.1uF, Capacitor_SMD:C_0402_1005Metric, F.Cu at (138.3, -87.0)
- added C83: 0.1uF, Capacitor_SMD:C_0402_1005Metric, F.Cu at (143.9, -91.0)
- added C84: 0.047uF, Capacitor_SMD:C_0402_1005Metric, F.Cu at (141.2, -87.0)
- added C85: 0.047uF, Capacitor_SMD:C_0402_1005Metric, F.Cu at (135.2, -89.7)
- added C86: 0.047uF, Capacitor_SMD:C_0402_1005Metric, F.Cu at (138.3, -85.1)
- added C87: 0.047uF, Capacitor_SMD:C_0402_1005Metric, F.Cu at (140.8, -95.0)
- added C88: 0.022uF, Capacitor_SMD:C_0402_1005Metric, F.Cu at (126.7, -85.1)
- added C89: 0.022uF, Capacitor_SMD:C_0402_1005Metric, F.Cu at (132.5, -85.7)
- added C9: 0.1uF, Capacitor_SMD:C_0603_1608Metric, F.Cu at (130.3, -32.7)
- added C90: 0.022uF, Capacitor_SMD:C_0402_1005Metric, F.Cu at (138.1, -93.0)
- added C91: 0.022uF, Capacitor_SMD:C_0402_1005Metric, F.Cu at (129.6, -83.1)
- added C92: 10uF/6.3V/0603, Capacitor_SMD:C_0603_1608Metric, F.Cu at (184.0, -78.9)
- added C93: 4.7uF/10V/0402, Capacitor_SMD:C_0402_1005Metric, F.Cu at (190.4, -81.6)
- added C94: 0.1uF/10V/0402, Capacitor_SMD:C_0402_1005Metric, F.Cu at (186.3, -76.6)
- added C95: 0.01uF/10V/0402, Capacitor_SMD:C_0402_1005Metric, F.Cu at (179.0, -75.7)
- added C96: 10uF/6.3V/0603, Capacitor_SMD:C_0603_1608Metric, F.Cu at (184.0, -81.4)
- added C97: 4.7uF/10V/0402, Capacitor_SMD:C_0402_1005Metric, F.Cu at (187.4, -81.6)
- added C98: 0.1uF/10V/0402, Capacitor_SMD:C_0402_1005Metric, F.Cu at (183.4, -76.6)
- added C99: 0.01uF/10V/0402, Capacitor_SMD:C_0402_1005Metric, F.Cu at (187.4, -79.6)
- added D1: SN74AVC4T774PWR, Package_SO:TSSOP-16_4.4x5mm_P0.65mm, F.Cu at (133.5, -0.40)
- added D2: SN74AVC4T774PWR, Package_SO:TSSOP-16_4.4x5mm_P0.65mm, F.Cu at (148.7, -0.40)
- added FB1: BLM15AX601SN1D, Inductor_SMD:L_0402_1005Metric, F.Cu at (150.6, -57.8)
- added FB11: MPZ2012S101AT000, Inductor_SMD:L_0805_2012Metric, F.Cu at (158.8, -52.8)
- added FB12: MPZ2012S101AT000, Inductor_SMD:L_0805_2012Metric, F.Cu at (158.8, -55.8)
- added FB13: MPZ2012S101AT000, Inductor_SMD:L_0805_2012Metric, F.Cu at (121.8, -77.0)
- added FB2: BLM15AX601SN1D, Inductor_SMD:L_0402_1005Metric, F.Cu at (150.6, -59.8)
- added FB3: MPZ2012S101AT000, Inductor_SMD:L_0805_2012Metric, F.Cu at (179.8, -81.1)
- added FB4: MPZ2012S101AT000, Inductor_SMD:L_0805_2012Metric, F.Cu at (179.8, -78.2)
- added FB5: MPZ2012S101AT000, Inductor_SMD:L_0805_2012Metric, F.Cu at (150.6, -94.5)
- added FB6: MPZ2012S101AT000, Inductor_SMD:L_0805_2012Metric, F.Cu at (150.6, -91.6)
- added FB7: MPZ2012S101AT000, Inductor_SMD:L_0805_2012Metric, F.Cu at (155.0, -94.5)
- added H1: PCB_HOLE, misc:PCIE104_HOLE, F.Cu at (53.9, -8.68)
- added H2: PCB_HOLE, misc:PCIE104_HOLE, F.Cu at (53.9, -16.0)
- added H3: PCB_HOLE, misc:PCIE104_HOLE, F.Cu at (46.6, -8.68)
- added H4: PCB_HOLE, misc:PCIE104_HOLE, F.Cu at (46.6, -16.0)
- added J10: 0473065005, OLIMEX_Connectors-FP:SATA-MALE-7, F.Cu at (76.5, -32.0)
- added J11: Conn_01x02, Connector_PinHeader_2.54mm:PinHeader_1x02_P2.54mm_Vertical, F.Cu at (179.9, -69.1)
- added J12: Conn_01x02, Connector_PinHeader_2.54mm:PinHeader_1x02_P2.54mm_Vertical, F.Cu at (158.8, -43.7)
- added J16: Conn_01x03, Connector_PinHeader_2.54mm:PinHeader_1x03_P2.54mm_Vertical, F.Cu at (177.0, -93.7)
- added J17: OneBank Bottom, samtec:ASP-129646-22, F.Cu at (78.8, -60.3)
- added J18: OneBank Top, samtec:ASP-129637-13, F.Cu at (78.3, -50.9)
- added J2: Conn_02x20_Odd_Even, Connector_PinHeader_1.27mm:PinHeader_2x20_P1.27mm_Vertical_SMD, F.Cu at (71.9, -82.3)
- added J4: Conn_01x02, Connector_PinHeader_2.54mm:PinHeader_1x02_P2.54mm_Vertical, F.Cu at (150.4, -76.1)
- added J5: Conn_01x02, Connector_PinHeader_2.54mm:PinHeader_1x02_P2.54mm_Vertical, F.Cu at (137.5, -61.0)
- added J7: Conn_01x02, Connector_PinHeader_2.54mm:PinHeader_1x02_P2.54mm_Vertical, F.Cu at (142.1, -61.0)
- added J8: Conn_01x02, Connector_PinHeader_2.54mm:PinHeader_1x02_P2.54mm_Vertical, F.Cu at (146.8, -61.0)
- added J9: 0473065005, OLIMEX_Connectors-FP:SATA-MALE-7, F.Cu at (116.5, -55.8)
- added Q1: FDV305N, Package_TO_SOT_SMD:TSOT-23, F.Cu at (110.4, -23.5)
- added Q2: FDV305N, Package_TO_SOT_SMD:TSOT-23, F.Cu at (182.0, -93.8)
- added R100: 10K, Resistor_SMD:R_0402_1005Metric, F.Cu at (198.6, -58.2)
- added R101: 10K, Resistor_SMD:R_0402_1005Metric, F.Cu at (198.6, -60.2)
- added R102: 10K, Resistor_SMD:R_0402_1005Metric, F.Cu at (198.6, -56.2)
- added R103: 10K, Resistor_SMD:R_0402_1005Metric, F.Cu at (198.9, -68.5)
- added R104: 10K, Resistor_SMD:R_0402_1005Metric, F.Cu at (198.9, -70.5)
- added R105: 10K, Resistor_SMD:R_0402_1005Metric, F.Cu at (201.8, -70.5)
- added R106: 10K, Resistor_SMD:R_0402_1005Metric, F.Cu at (198.9, -66.5)
- added R107: 22R, Resistor_SMD:R_0402_1005Metric, F.Cu at (130.3, -40.6)
- added R108: 4K7, Resistor_SMD:R_0603_1608Metric, F.Cu at (184.2, -70.2)
- added R109: 4K7, Resistor_SMD:R_0603_1608Metric, F.Cu at (163.1, -44.8)
- added R110: 10K, Resistor_SMD:R_0603_1608Metric, F.Cu at (115.1, -24.5)
- added R112: 22R, Resistor_SMD:R_0402_1005Metric, F.Cu at (200.5, -93.0)
- added R114: 22R, Resistor_SMD:R_0402_1005Metric, F.Cu at (200.5, -95.0)
- added R115: 22R, Resistor_SMD:R_0402_1005Metric, F.Cu at (197.6, -93.0)
- added R116: 22R, Resistor_SMD:R_0402_1005Metric, F.Cu at (197.6, -95.0)
- added R141: 10K, Resistor_SMD:R_0603_1608Metric, F.Cu at (186.7, -94.7)
- added R144: 10K, Resistor_SMD:R_0603_1608Metric, F.Cu at (181.4, -90.3)
- added R145: DNP, chip_rlc:r_0402, F.Cu at (64.5, -18.8)
- added R146: 10K, chip_rlc:r_0402, F.Cu at (61.7, -18.8)
- added R147: 10K, chip_rlc:r_0402, F.Cu at (59.0, -18.8)
- renumbered C14 to C128, C16 to C129, C2 to C130, C15 to C131, C17 to C132, C1 to C133, C3 to C134, C12 to C135, C4 to C136, C7 to C137, C10 to C138, C5 to C139, C8 to C140, C11 to C141, C13 to C142, C6 to C143, C9 to C144, FB3 to FB10, FB1 to FB8, FB2 to FB9, J2 to J13, J5 to J14, J4 to J15, R3 to R111, R4 to R113, R5 to R117, R6 to R118, R7 to R119, R9 to R120, R8 to R121, R55 to R122, R31 to R123, R32 to R124, R33 to R125, R34 to R126, R35 to R127, R36 to R128, R37 to R129, R38 to R130, R39 to R131, R40 to R132, R41 to R133, R42 to R134, R43 to R135, R44 to R136, R45 to R137, R46 to R138, R56 to R139, R57 to R140, R58 to R142, R47 to R143, U1 to U14, U2 to U15, Y1 to Y2
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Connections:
- net /CPU/DEBUG/CPU_EJTAG/EJTAG20_Conn/DBGRQ renamed /CPU/CPU_DEBUG/CPU_EJTAG/EJTAG20_Conn/DBGRQ
- net /CPU/DEBUG/CPU_EJTAG/EJTAG20_Conn/TCK renamed /CPU/CPU_DEBUG/CPU_EJTAG/EJTAG20_Conn/TCK
- net /CPU/DEBUG/CPU_EJTAG/EJTAG20_Conn/TDI renamed /CPU/CPU_DEBUG/CPU_EJTAG/EJTAG20_Conn/TDI
- net /CPU/DEBUG/CPU_EJTAG/EJTAG20_Conn/TDO renamed /CPU/CPU_DEBUG/CPU_EJTAG/EJTAG20_Conn/TDO
- net /CPU/DEBUG/CPU_EJTAG/EJTAG20_Conn/TMS renamed /CPU/CPU_DEBUG/CPU_EJTAG/EJTAG20_Conn/TMS
- net /CPU/DEBUG/CPU_EJTAG/EJTAG20_Conn/nTRST renamed /CPU/CPU_DEBUG/CPU_EJTAG/EJTAG20_Conn/nTRST
- net /CPU/DEBUG/CPU_JTAG/JTAG20_Conn/DBGRQ renamed /CPU/CPU_DEBUG/CPU_JTAG/JTAG20_Conn/DBGRQ
- net /CPU/DEBUG/CPU_JTAG/JTAG20_Conn/TCK renamed /CPU/CPU_DEBUG/CPU_JTAG/JTAG20_Conn/TCK
- net /CPU/DEBUG/CPU_JTAG/JTAG20_Conn/TDI renamed /CPU/CPU_DEBUG/CPU_JTAG/JTAG20_Conn/TDI
- net /CPU/DEBUG/CPU_JTAG/JTAG20_Conn/TDO renamed /CPU/CPU_DEBUG/CPU_JTAG/JTAG20_Conn/TDO
- net /CPU/DEBUG/CPU_JTAG/JTAG20_Conn/TMS renamed /CPU/CPU_DEBUG/CPU_JTAG/JTAG20_Conn/TMS
- net /CPU/DEBUG/CPU_JTAG/JTAG20_Conn/nTRST renamed /CPU/CPU_DEBUG/CPU_JTAG/JTAG20_Conn/nTRST
- net /CPU/DEBUG/CPU_TRACE/TR_CLK renamed /CPU/CPU_DEBUG/CPU_TRACE/TR_CLK
- net /CPU/DEBUG/CPU_TRACE/TR_DATA0 renamed /CPU/CPU_DEBUG/CPU_TRACE/TR_DATA0
- net /CPU/DEBUG/CPU_TRACE/TR_DATA1 renamed /CPU/CPU_DEBUG/CPU_TRACE/TR_DATA1
- net /CPU/DEBUG/CPU_TRACE/TR_DATA10 renamed /CPU/CPU_DEBUG/CPU_TRACE/TR_DATA10
- net /CPU/DEBUG/CPU_TRACE/TR_DATA11 renamed /CPU/CPU_DEBUG/CPU_TRACE/TR_DATA11
- net /CPU/DEBUG/CPU_TRACE/TR_DATA12 renamed /CPU/CPU_DEBUG/CPU_TRACE/TR_DATA12
- net /CPU/DEBUG/CPU_TRACE/TR_DATA13 renamed /CPU/CPU_DEBUG/CPU_TRACE/TR_DATA13
- net /CPU/DEBUG/CPU_TRACE/TR_DATA14 renamed /CPU/CPU_DEBUG/CPU_TRACE/TR_DATA14
- net /CPU/DEBUG/CPU_TRACE/TR_DATA15 renamed /CPU/CPU_DEBUG/CPU_TRACE/TR_DATA15
- net /CPU/DEBUG/CPU_TRACE/TR_DATA2 renamed /CPU/CPU_DEBUG/CPU_TRACE/TR_DATA2
- net /CPU/DEBUG/CPU_TRACE/TR_DATA3 renamed /CPU/CPU_DEBUG/CPU_TRACE/TR_DATA3
- net /CPU/DEBUG/CPU_TRACE/TR_DATA4 renamed /CPU/CPU_DEBUG/CPU_TRACE/TR_DATA4
- net /CPU/DEBUG/CPU_TRACE/TR_DATA5 renamed /CPU/CPU_DEBUG/CPU_TRACE/TR_DATA5
- net /CPU/DEBUG/CPU_TRACE/TR_DATA6 renamed /CPU/CPU_DEBUG/CPU_TRACE/TR_DATA6
- net /CPU/DEBUG/CPU_TRACE/TR_DATA7 renamed /CPU/CPU_DEBUG/CPU_TRACE/TR_DATA7
- net /CPU/DEBUG/CPU_TRACE/TR_DATA8 renamed /CPU/CPU_DEBUG/CPU_TRACE/TR_DATA8
- net /CPU/DEBUG/CPU_TRACE/TR_DATA9 renamed /CPU/CPU_DEBUG/CPU_TRACE/TR_DATA9
- net /CPU/DEBUG/CPU_TRACE/TR_DM renamed /CPU/CPU_DEBUG/CPU_TRACE/TR_DM
- net /CPU/DEBUG/CPU_TRACE/TR_PROBE_N renamed /CPU/CPU_DEBUG/CPU_TRACE/TR_PROBE_N
- net /CPU/DEBUG/CPU_TRACE/TR_TEST renamed /CPU/CPU_DEBUG/CPU_TRACE/TR_TEST
- net /CPU/DEBUG/CPU_TRACE/TR_TRIGIN renamed /CPU/CPU_DEBUG/CPU_TRACE/TR_TRIGIN
- net /CPU/DEBUG/CPU_TRACE/TR_TRIGOUT renamed /CPU/CPU_DEBUG/CPU_TRACE/TR_TRIGOUT
- net /CPU/DEBUG/CPU_TRACE/TSTSEL_3 renamed /CPU/CPU_DEBUG/CPU_TRACE/TSTSEL_3
- net /CPU/ULPI/EXTBUS_FLG renamed /CPU/CPU_ULPI/EXTBUS_FLG
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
